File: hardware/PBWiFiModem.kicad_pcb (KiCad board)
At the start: 2 copper layers, 92 x 37 mm, 20 parts, among them J1 Conn_02x10_Odd_Even, J2 Conn_01x06_Pin, U1 LM1117MP-3.3, U2 TXS0108EPW, U3 ESP-12F

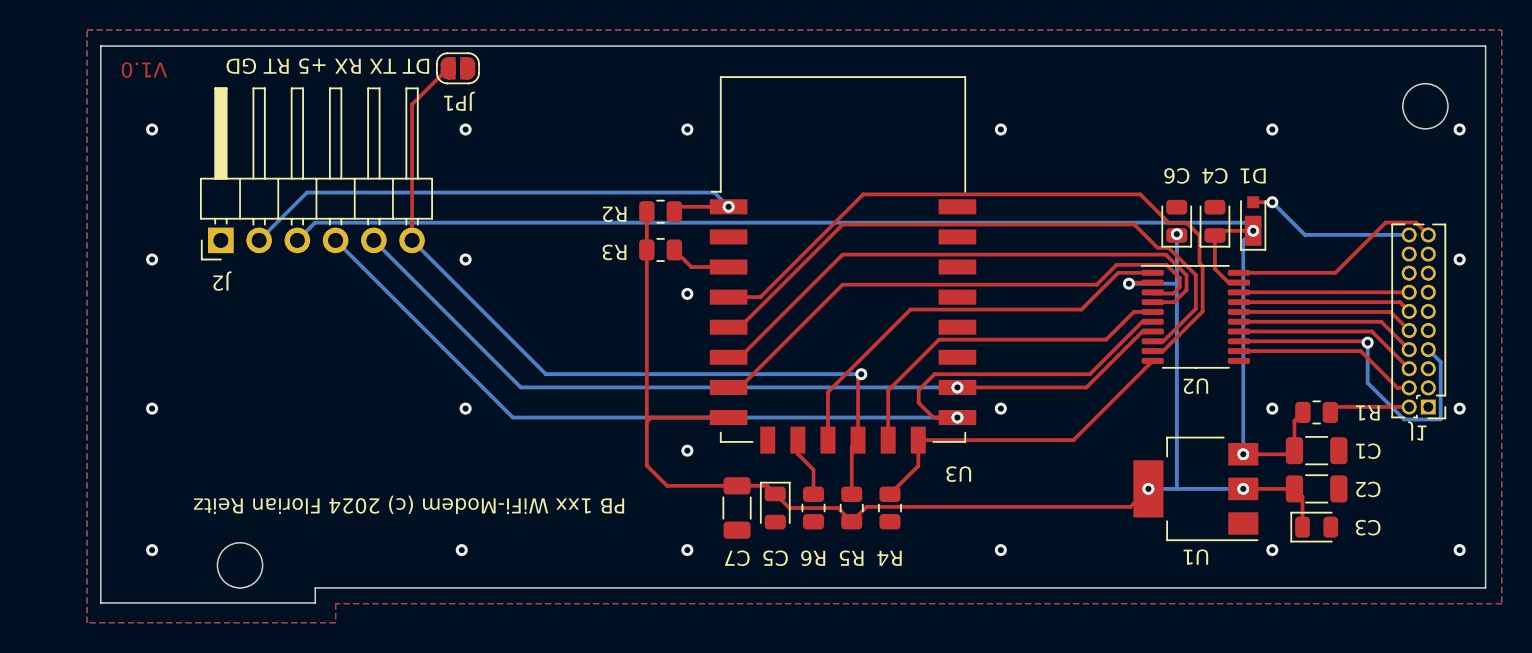
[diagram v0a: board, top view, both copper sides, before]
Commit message: Connector changed to SMD
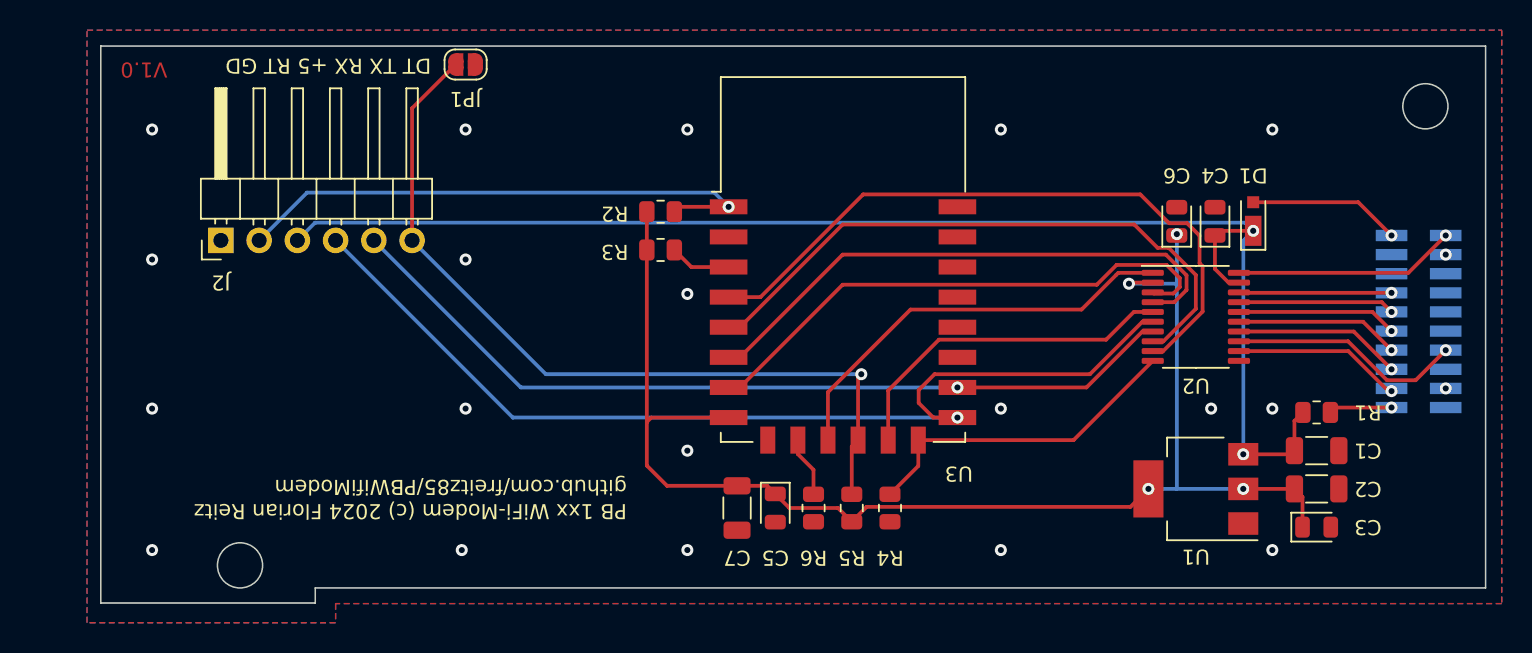
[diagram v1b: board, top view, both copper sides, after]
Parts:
- J1: footprint Connector_PinHeader_1.27mm:PinHeader_2x10_P1.27mm_Vertical -> Connector_PinSocket_1.27mm:PinSocket_2x10_P1.27mm_Vertical_SMD; moved to B.Cu
- moved J1 5.71 mm to (178.3, 108.8), turned to 0 degrees
- moved JP1 0.57 mm to (115.0, 91.7)
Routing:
- net ~{RI.DETECT}: track 22.1 -> 15.6 mm
- net ~{DTR}: track 11.8 -> 10.7 mm, vias 0 -> 1
- net MODEM.5V: track 11.3 -> 10.1 mm
- net RxD: track 12.3 -> 11.2 mm, vias 0 -> 1
- net ~{RTS}: track 11.6 -> 10.4 mm, vias 0 -> 1
- net TxD: track 12.1 -> 10.9 mm, vias 0 -> 1
- net ~{CTS}: track 11.3 -> 10.2 mm, vias 0 -> 1
- net ~{MODEM.BUSY}: track 12.3 -> 11.2 mm, vias 0 -> 1
- net MODEM.PWR: track 5.55 -> 4.71 mm, vias 0 -> 1
- net ~{DCD}: track 14.3 -> 14.8 mm, vias 0 -> 1
- net GND: vias 22 -> 21
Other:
- board text added: "PB 1xx WiFi-Modem (c) 2024 Florian Reitz github.com/freitz85/PBWifiModem"
- board text removed: "PB 1xx WiFi-Modem (c) 2024 Florian Reitz"
